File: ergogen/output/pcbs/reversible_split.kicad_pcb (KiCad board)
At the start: 2 copper layers, 142.6 x 97.7 mm, 19 parts

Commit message: Tighter outline
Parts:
- moved MCU1 3.64 mm to (240.3, 76.3)
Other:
- board size 142.6 x 97.7 mm -> 140.7 x 97.7 mm

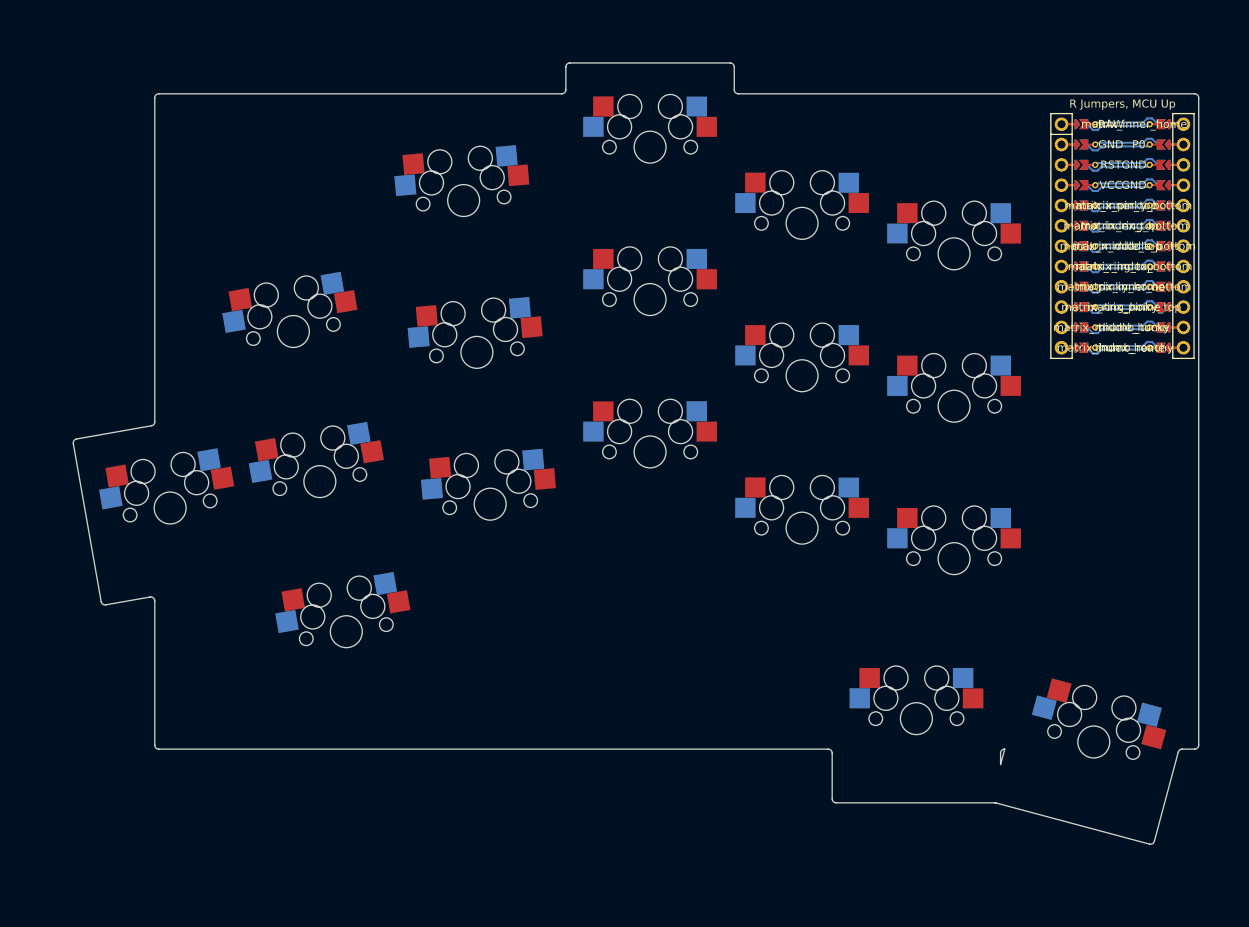
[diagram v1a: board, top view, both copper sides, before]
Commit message: First complete layout
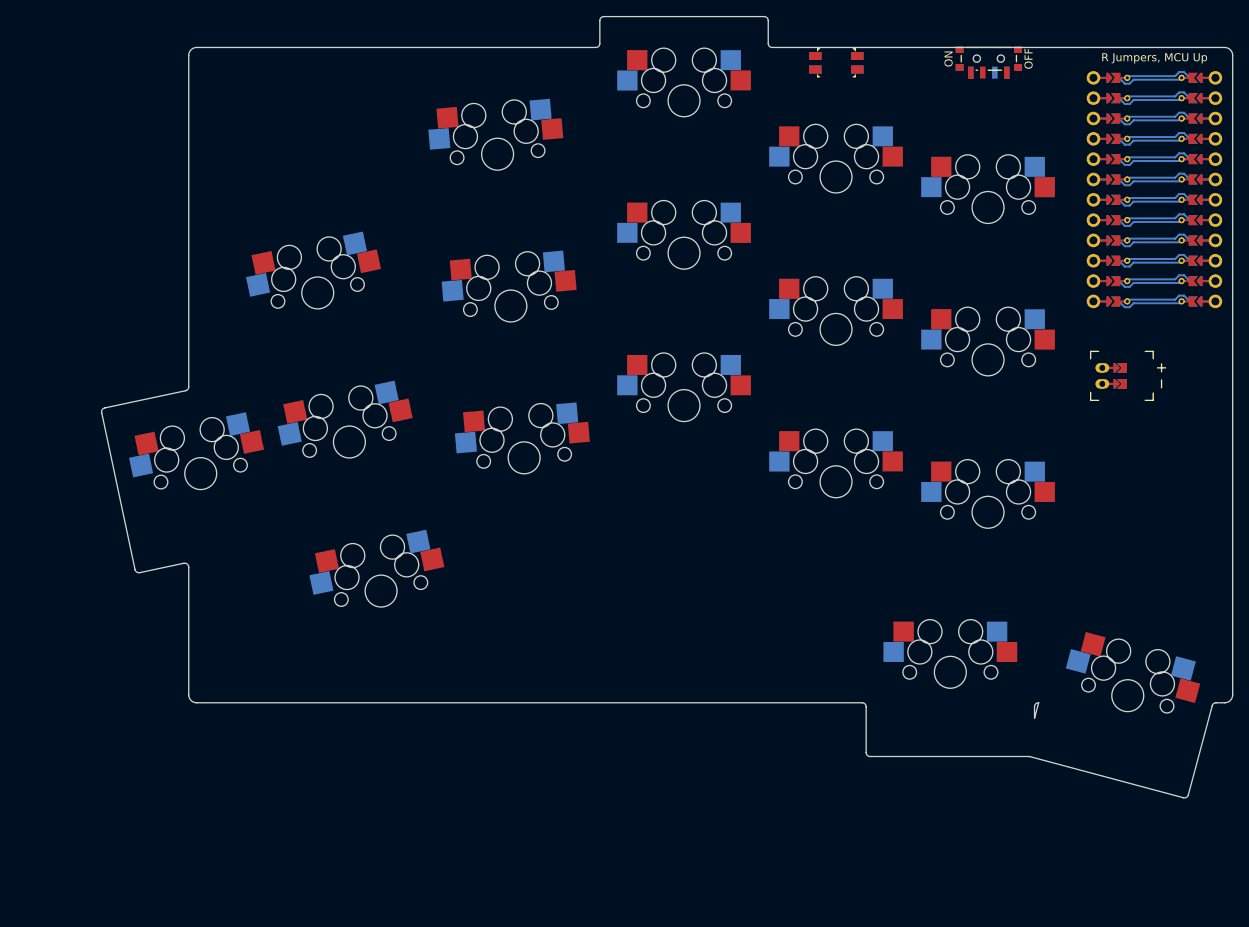
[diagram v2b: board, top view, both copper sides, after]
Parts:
- added JST1: , ceoloide:battery_connector_jst_ph_2, F.Cu at (237.7, 95.1)
- added PWR1: , ceoloide:power_switch_smd_side, F.Cu at (223.6, 55.4)
- added RST1: , ceoloide:reset_switch_smd_side, F.Cu at (204.5, 55.9)
- moved S8 7.18 mm to (185.5, 98.8)
- moved S9 7.18 mm to (185.5, 79.7)
- moved S10 7.18 mm to (185.5, 60.7)
- moved S12 7.18 mm to (204.5, 89.3)
- moved S17 7.18 mm to (218.7, 132.1)
- moved S18 7.18 mm to (240.9, 135.1)
- moved S6 7.18 mm to (163.8, 86.3)
- moved S7 7.18 mm to (162.1, 67.4)
- moved S11 7.18 mm to (204.5, 108.3)
- moved S5 7.18 mm to (165.5, 105.3)
- moved S14 7.18 mm to (223.5, 112.1)
- moved S15 7.18 mm to (223.5, 93.1)
- moved S13 7.18 mm to (204.5, 70.2)
- moved S16 7.18 mm to (223.5, 74.0)
- moved MCU1 7.04 mm to (244.3, 70.5)
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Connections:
- MCU1 pad 101: matrix_inner_home -> matrix_outer_home
- MCU1 pad 102: P0 -> matrix_pinky_top
- MCU1 pad 105: matrix_pinky_bottom -> matrix_pinky_home
- MCU1 pad 106: matrix_ring_bottom -> matrix_pinky_bottom
- MCU1 pad 107: matrix_middle_bottom -> matrix_ring_top
- MCU1 pad 108: matrix_index_bottom -> matrix_ring_home
- MCU1 pad 109: matrix_inner_bottom -> matrix_ring_bottom
- MCU1 pad 110: matrix_pinky_top -> matrix_middle_top
- MCU1 pad 111: thumb_tucky -> matrix_middle_home
- MCU1 pad 112: thumb_reachy -> matrix_middle_bottom
- MCU1 pad 113: matrix_index_home -> thumb_tucky
- MCU1 pad 114: matrix_middle_home -> thumb_reachy
- MCU1 pad 115: matrix_ring_home -> matrix_index_home
- MCU1 pad 116: matrix_pinky_home -> matrix_inner_home
- MCU1 pad 117: matrix_ring_top -> matrix_inner_top
- MCU1 pad 118: matrix_middle_top -> matrix_inner_bottom
- MCU1 pad 119: matrix_index_top -> matrix_inner_home
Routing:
- net JST1_2: track 0.00 -> 3.60 mm
- net JST1_1: track 0.00 -> 3.60 mm
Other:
- board size 140.7 x 97.7 mm -> 141.4 x 97.7 mm

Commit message: Rotated layout experiment
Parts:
- moved S18 25.0 mm to (220.7, 149.8), turned to -10 degrees
- moved S17 22.1 mm to (202.0, 146.5), turned to -10 degrees
- moved PWR1 20.1 mm to (217.9, 74.7), turned to 85 degrees
- moved JST1 18.8 mm to (228.9, 111.6), turned to 85 degrees
- moved MCU1 18.5 mm to (237.5, 87.8), turned to -5 degrees
- moved RST1 18.5 mm to (198.9, 73.6), turned to -5 degrees
- moved S11 18.5 mm to (194.4, 123.8), turned to -5 degrees
- moved S14 18.4 mm to (213.2, 127.4), turned to -5 degrees
- moved S8 18.3 mm to (176.1, 114.6), turned to -5 degrees
- moved S12 17.7 mm to (196.1, 104.9), turned to -5 degrees
- moved S9 17.6 mm to (177.8, 95.6), turned to -5 degrees
- moved S15 17.6 mm to (214.8, 108.4), turned to -5 degrees
- moved S5 17.1 mm to (155.7, 119.3), turned to 0 degrees
- moved S13 17.0 mm to (197.7, 85.9), turned to -5 degrees
- moved S10 17.0 mm to (179.5, 76.6), turned to -5 degrees
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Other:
- board size 141.4 x 97.7 mm -> 129.9 x 96.6 mm

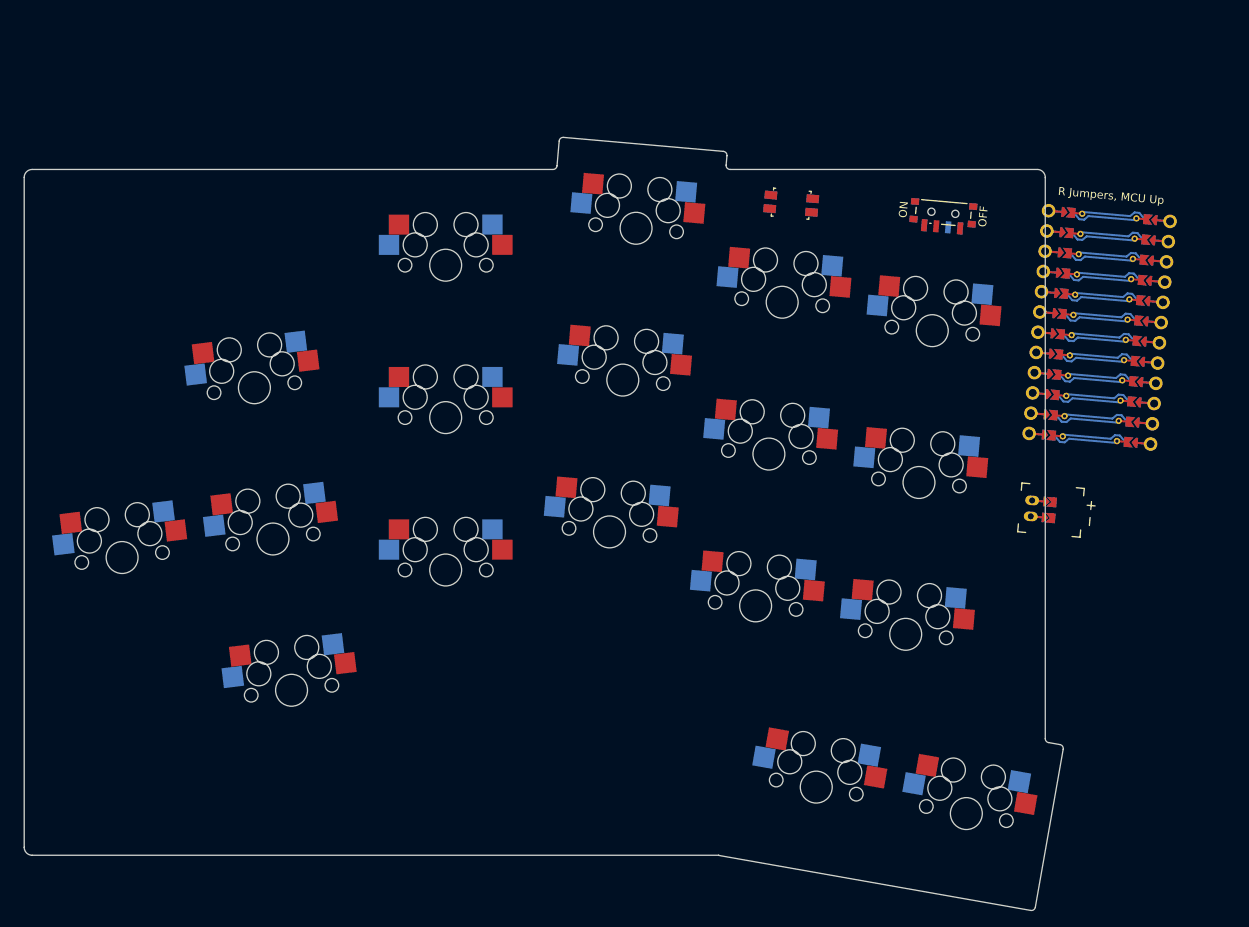
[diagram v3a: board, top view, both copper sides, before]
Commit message: Updated SMD positions
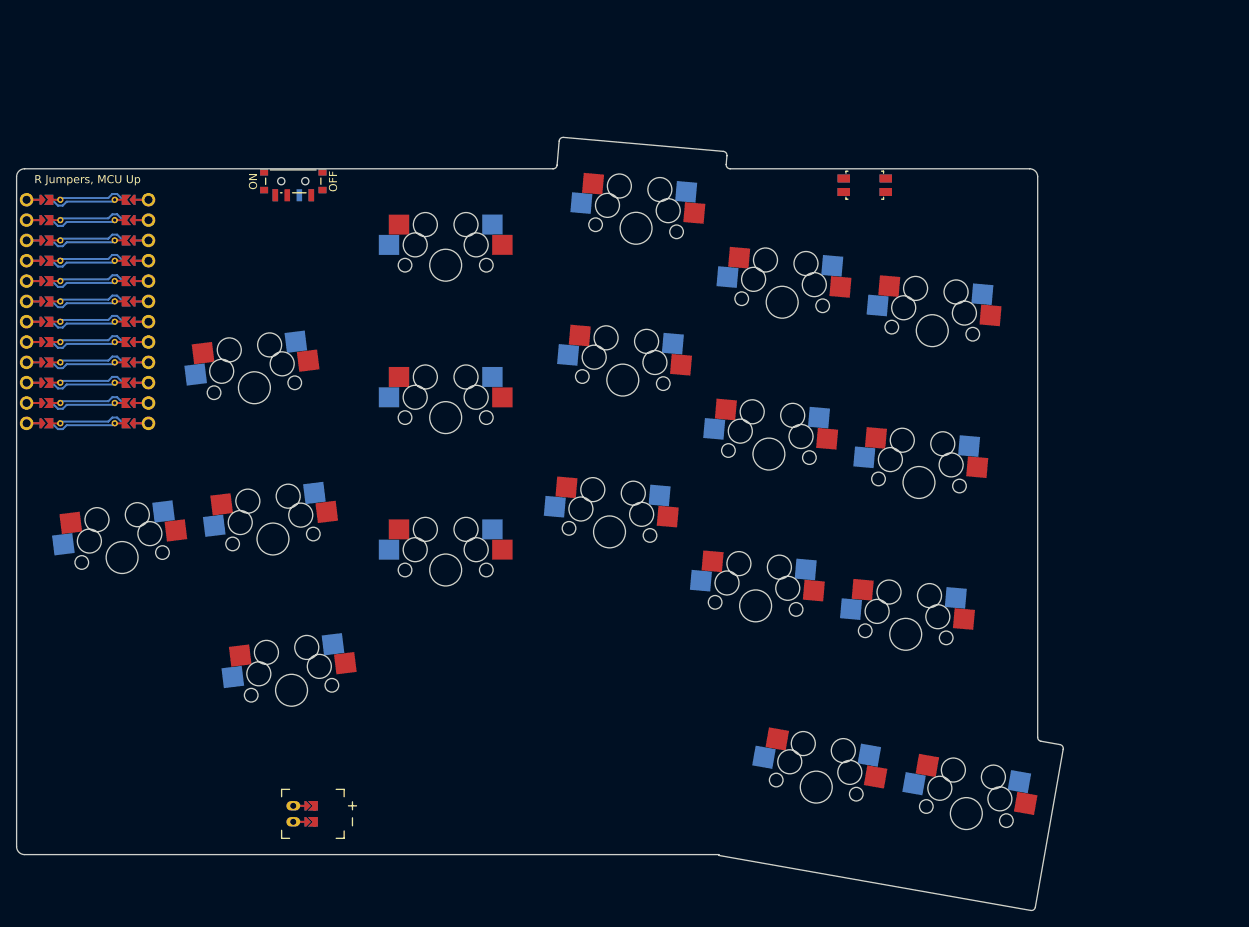
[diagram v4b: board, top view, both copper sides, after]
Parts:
- moved MCU1 126.6 mm to (110.9, 85.8), turned to 0 degrees
- moved JST1 99.9 mm to (136.6, 149.8), turned to 90 degrees
- moved PWR1 81.4 mm to (136.6, 70.8), turned to 90 degrees
- moved RST1 9.48 mm to (208.0, 71.2), turned to 0 degrees
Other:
- board size 129.9 x 96.6 mm -> 130.8 x 96.6 mm

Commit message: First Complete PCB
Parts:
- added H1: , ceoloide:mounting_hole_plated, F.Cu at (136.6, 79.3)
- added H2: , ceoloide:mounting_hole_plated, F.Cu at (117.5, 136.7)
- added H3: , ceoloide:mounting_hole_plated, F.Cu at (226.8, 135.3)
- added H4: , ceoloide:mounting_hole_plated, F.Cu at (217.9, 73.3)
- moved S17 0.95 mm to (201.0, 146.4)
- moved S18 0.95 mm to (219.8, 149.7)
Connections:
- MCU1 pad 101: matrix_outer_home -> matrix_ring_top
- MCU1 pad 102: matrix_pinky_top -> matrix_middle_bottom
- MCU1 pad 105: matrix_pinky_home -> matrix_middle_home
- MCU1 pad 106: matrix_pinky_bottom -> matrix_middle_top
- MCU1 pad 107: matrix_ring_top -> matrix_index_bottom
- MCU1 pad 108: matrix_ring_home -> matrix_index_home
- MCU1 pad 109: matrix_ring_bottom -> matrix_index_top
- MCU1 pad 110: matrix_middle_top -> matrix_inner_bottom
- MCU1 pad 111: matrix_middle_home -> matrix_inner_home
- MCU1 pad 112: matrix_middle_bottom -> matrix_inner_top
- MCU1 pad 113: thumb_tucky -> thumb_reachy
- MCU1 pad 114: thumb_reachy -> thumb_tucky
- MCU1 pad 115: matrix_index_home -> matrix_outer_home
- MCU1 pad 116: matrix_inner_home -> matrix_pinky_bottom
- MCU1 pad 117: matrix_inner_top -> matrix_pinky_home
- MCU1 pad 118: matrix_inner_bottom -> matrix_pinky_top
- MCU1 pad 119: matrix_inner_home -> matrix_ring_bottom
- MCU1 pad 120: matrix_inner_top -> matrix_ring_home
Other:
- board size 130.8 x 96.6 mm -> 129.9 x 96.6 mm
- board text added: "SplayBreak v1.0.0"
